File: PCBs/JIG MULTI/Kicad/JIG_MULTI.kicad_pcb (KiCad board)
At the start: 2 copper layers, 107.9 x 78.7 mm, 19 parts, among them U1 Vita_Connector, U2 12pad, U3 12pad

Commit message: fixed silkscreen typo
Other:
- board text added: "5V R1 = 1K R2 = 1K R3 = 1K R4 = 150 R5 = 2K R6 = 7.5K"
- board text removed: "5V R1 = 1K R2 = 1K R3 = 1K R4 = 150 R5 = 2K R5 = 7.5K"
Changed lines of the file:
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@@
   (gr_rect (start 31.75 30.48) (end 139.7 109.22)
     (stroke (width 0.1) (type default)) (fill none) (layer "Edge.Cuts"))
-  (gr_text "5V\nR1 = 1K\nR2 = 1K\nR3 = 1K\nR4 = 150\nR5 = 2K\nR5 = 7.5K" (at 134.62 55.88) (layer "B.SilkS")
+  (gr_text "5V\nR1 = 1K\nR2 = 1K\nR3 = 1K\nR4 = 150\nR5 = 2K\nR6 = 7.5K" (at 134.62 55.88) (layer "B.SilkS")
     (effects (font (size 2 2) (thickness 0.1)) (justify left bottom mirror))
   )
@@
     (effects (font (size 1 1) (thickness 0.2)) (justify left bottom))
   )
-  (gr_text "5V\nR1 = 1K\nR2 = 1K\nR3 = 1K\nR4 = 150\nR5 = 2K\nR5 = 7.5K" (at 121.92 106.68) (layer "F.SilkS")
+  (gr_text "5V\nR1 = 1K\nR2 = 1K\nR3 = 1K\nR4 = 150\nR5 = 2K\nR6 = 7.5K" (at 121.92 106.68) (layer "F.SilkS")
     (effects (font (size 2 2) (thickness 0.1)) (justify left bottom))
   )

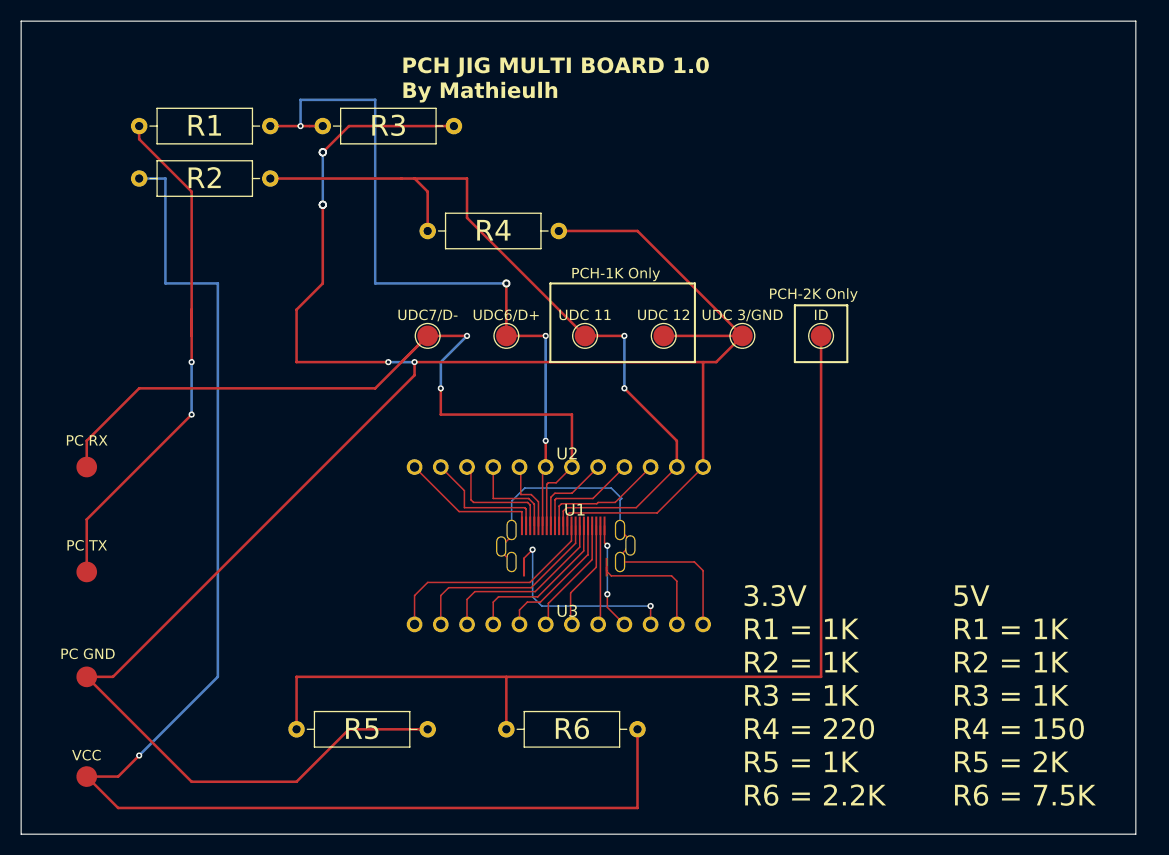
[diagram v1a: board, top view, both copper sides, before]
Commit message: smaller footprint
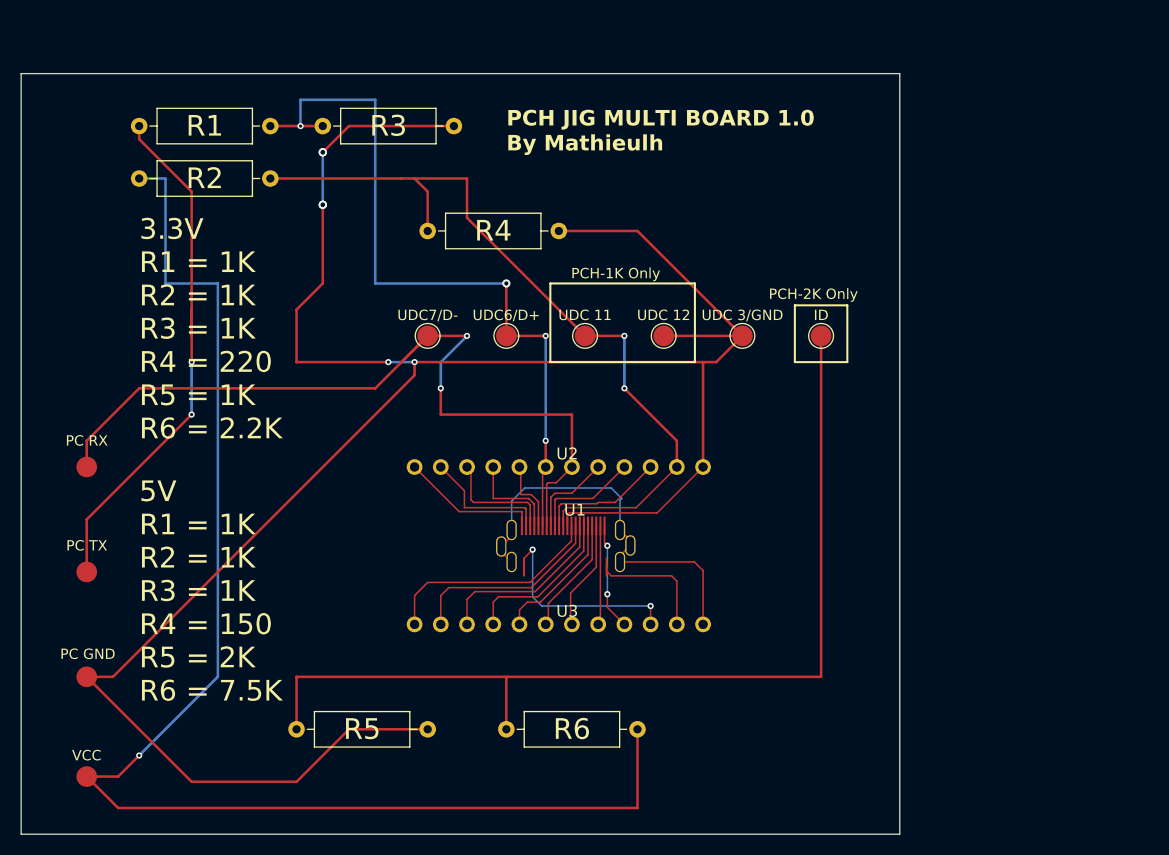
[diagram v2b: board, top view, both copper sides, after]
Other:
- board size 107.9 x 78.7 mm -> 85.1 x 73.7 mm
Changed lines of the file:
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@@
   (gr_rect (start 83 55.88) (end 97 63.5)
     (stroke (width 0.2) (type default)) (fill none) (layer "F.SilkS"))
-  (gr_rect (start 31.75 30.48) (end 139.7 109.22)
+  (gr_rect (start 31.75 35.56) (end 116.84 109.22)
     (stroke (width 0.1) (type default)) (fill none) (layer "Edge.Cuts"))
-  (gr_text "5V\nR1 = 1K\nR2 = 1K\nR3 = 1K\nR4 = 150\nR5 = 2K\nR6 = 7.5K" (at 134.62 55.88) (layer "B.SilkS")
+  (gr_text "5V\nR1 = 1K\nR2 = 1K\nR3 = 1K\nR4 = 150\nR5 = 2K\nR6 = 7.5K" (at 106.68 93.98) (layer "B.SilkS")
     (effects (font (size 2 2) (thickness 0.1)) (justify left bottom mirror))
   )
-  (gr_text "3.3V\nR1 = 1K\nR2 = 1K	\nR3 = 1K\nR4 = 220\nR5 = 1K\nR6 = 2.2K" (at 114.3 55.88) (layer "B.SilkS")
+  (gr_text "3.3V\nR1 = 1K\nR2 = 1K	\nR3 = 1K\nR4 = 220\nR5 = 1K\nR6 = 2.2K" (at 86.36 93.98) (layer "B.SilkS")
     (effects (font (size 2 2) (thickness 0.1)) (justify left bottom mirror))
   )
@@
     (effects (font (size 1 1) (thickness 0.2)) (justify left bottom))
   )
-  (gr_text "5V\nR1 = 1K\nR2 = 1K\nR3 = 1K\nR4 = 150\nR5 = 2K\nR6 = 7.5K" (at 121.92 106.68) (layer "F.SilkS")
+  (gr_text "5V\nR1 = 1K\nR2 = 1K\nR3 = 1K\nR4 = 150\nR5 = 2K\nR6 = 7.5K" (at 43.18 96.52) (layer "F.SilkS")
     (effects (font (size 2 2) (thickness 0.1)) (justify left bottom))
   )
@@
     (effects (font (size 1 1) (thickness 0.2)) (justify left bottom))
   )
-  (gr_text "3.3V\nR1 = 1K\nR2 = 1K	\nR3 = 1K\nR4 = 220\nR5 = 1K\nR6 = 2.2K" (at 101.6 106.68) (layer "F.SilkS")
+  (gr_text "3.3V\nR1 = 1K\nR2 = 1K	\nR3 = 1K\nR4 = 220\nR5 = 1K\nR6 = 2.2K" (at 43.18 71.12) (layer "F.SilkS")
     (effects (font (size 2 2) (thickness 0.1)) (justify left bottom))
   )
@@
     (effects (font (size 1 1) (thickness 0.15)))
   )
-  (gr_text "PCH JIG MULTI BOARD 1.0\nBy Mathieulh" (at 68.58 38.1) (layer "F.SilkS")
+  (gr_text "PCH JIG MULTI BOARD 1.0\nBy Mathieulh" (at 78.74 43.18) (layer "F.SilkS")
     (effects (font (size 1.5 1.5) (thickness 0.3) bold) (justify left bottom))
   )

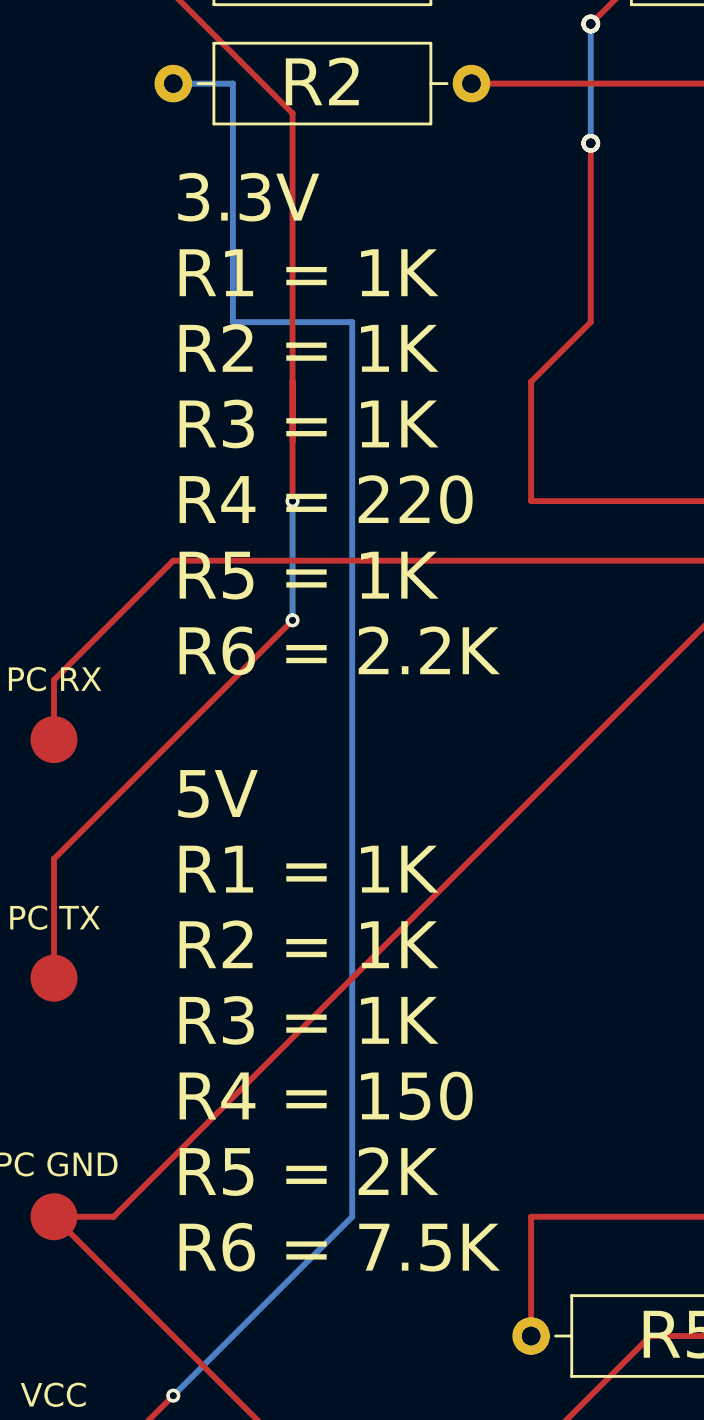
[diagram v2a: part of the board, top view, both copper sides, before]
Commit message: better silkscreen placement
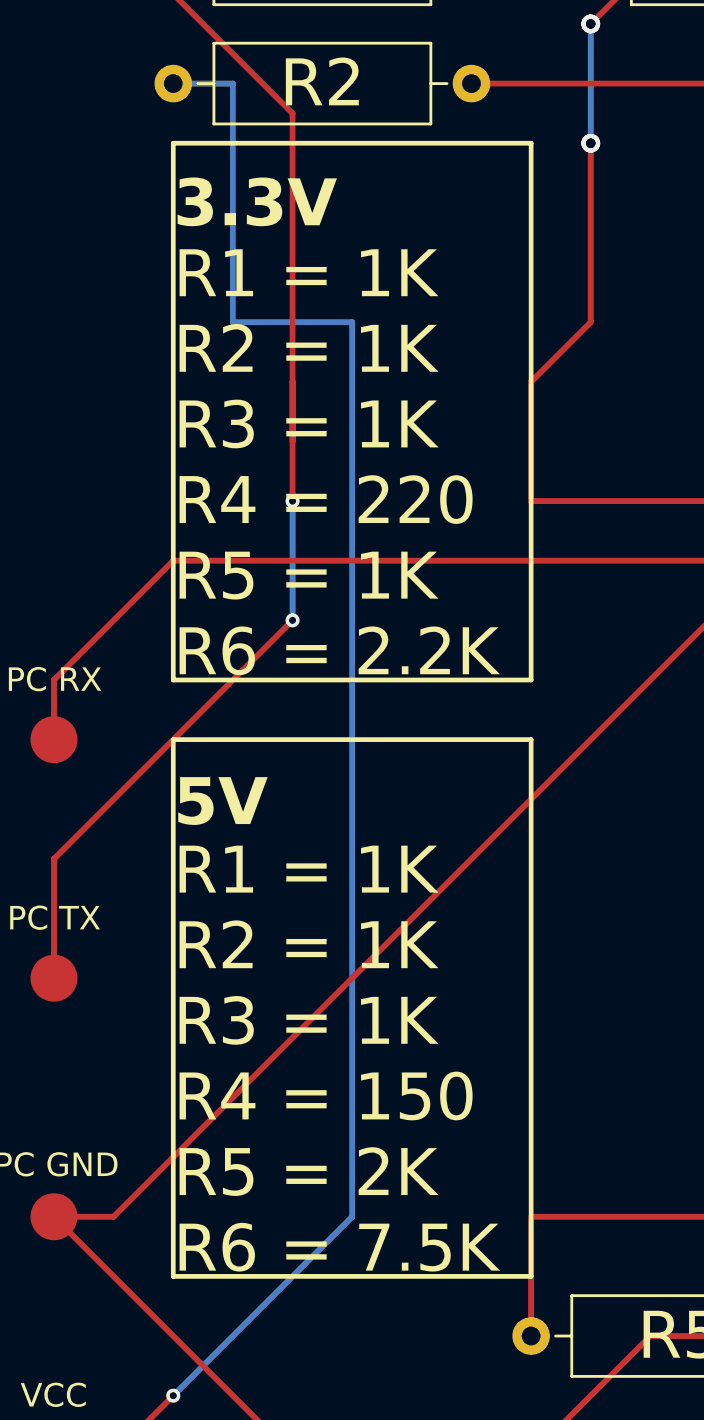
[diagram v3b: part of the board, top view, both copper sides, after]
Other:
- board text added: "3.3V"
- board text added: "5V"
- board text added: "R1 = 1K R2 = 1K R3 = 1K R4 = 150 R5 = 2K R6 = 7.5K"
- board text added: "R1 = 1K R2 = 1K R3 = 1K R4 = 220 R5 = 1K R6 = 2.2K"
- board text removed: "3.3V R1 = 1K R2 = 1K R3 = 1K R4 = 220 R5 = 1K R6 = 2.2K"
- board text removed: "5V R1 = 1K R2 = 1K R3 = 1K R4 = 150 R5 = 2K R6 = 7.5K"
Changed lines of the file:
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@@
   (gr_line (start 58.42 93.98) (end 58.42 99.06)
     (stroke (width 0.25) (type default)) (layer "F.Cu"))
+  (gr_rect (start 91.44 73.66) (end 106.68 96.52)
+    (stroke (width 0.2) (type default)) (fill none) (layer "B.SilkS"))
+  (gr_rect (start 91.44 48.26) (end 106.68 71.12)
+    (stroke (width 0.2) (type default)) (fill none) (layer "B.SilkS"))
   (gr_rect (start 106.68 58) (end 111.76 63.5)
+    (stroke (width 0.2) (type default)) (fill none) (layer "F.SilkS"))
+  (gr_rect (start 43.18 73.66) (end 58.42 96.52)
+    (stroke (width 0.2) (type default)) (fill none) (layer "F.SilkS"))
+  (gr_rect (start 43.18 48.26) (end 58.42 71.12)
     (stroke (width 0.2) (type default)) (fill none) (layer "F.SilkS"))
   (gr_rect (start 83 55.88) (end 97 63.5)
@@
   (gr_rect (start 31.75 35.56) (end 116.84 109.22)
     (stroke (width 0.1) (type default)) (fill none) (layer "Edge.Cuts"))
-  (gr_text "5V\nR1 = 1K\nR2 = 1K\nR3 = 1K\nR4 = 150\nR5 = 2K\nR6 = 7.5K" (at 106.68 93.98) (layer "B.SilkS")
+  (gr_text "5V" (at 106.68 77.5) (layer "B.SilkS")
+    (effects (font (size 2 2) (thickness 0.4) bold) (justify left bottom mirror))
+  )
+  (gr_text "R1 = 1K\nR2 = 1K\nR3 = 1K\nR4 = 150\nR5 = 2K\nR6 = 7.5K" (at 106.68 96.52) (layer "B.SilkS")
     (effects (font (size 2 2) (thickness 0.1)) (justify left bottom mirror))
   )
-  (gr_text "3.3V\nR1 = 1K\nR2 = 1K	\nR3 = 1K\nR4 = 220\nR5 = 1K\nR6 = 2.2K" (at 86.36 93.98) (layer "B.SilkS")
+  (gr_text "R1 = 1K\nR2 = 1K	\nR3 = 1K\nR4 = 220\nR5 = 1K\nR6 = 2.2K" (at 106.68 71.12) (layer "B.SilkS")
     (effects (font (size 2 2) (thickness 0.1)) (justify left bottom mirror))
+  )
+  (gr_text "3.3V" (at 106.68 52) (layer "B.SilkS")
+    (effects (font (size 2 2) (thickness 0.4) bold) (justify left bottom mirror))
   )
   (gr_text "PC GND" (at 38.202681 91.783349) (layer "F.SilkS")
@@
     (effects (font (size 1 1) (thickness 0.2)) (justify left bottom))
   )
-  (gr_text "5V\nR1 = 1K\nR2 = 1K\nR3 = 1K\nR4 = 150\nR5 = 2K\nR6 = 7.5K" (at 43.18 96.52) (layer "F.SilkS")
+  (gr_text "R1 = 1K\nR2 = 1K\nR3 = 1K\nR4 = 150\nR5 = 2K\nR6 = 7.5K" (at 43.18 96.52) (layer "F.SilkS")
     (effects (font (size 2 2) (thickness 0.1)) (justify left bottom))
   )
@@
     (effects (font (size 1 1) (thickness 0.2)) (justify left bottom))
   )
-  (gr_text "3.3V\nR1 = 1K\nR2 = 1K	\nR3 = 1K\nR4 = 220\nR5 = 1K\nR6 = 2.2K" (at 43.18 71.12) (layer "F.SilkS")
+  (gr_text "R1 = 1K\nR2 = 1K	\nR3 = 1K\nR4 = 220\nR5 = 1K\nR6 = 2.2K" (at 43.18 71.12) (layer "F.SilkS")
     (effects (font (size 2 2) (thickness 0.1)) (justify left bottom))
   )
   (gr_text "PC TX" (at 38.1 81.28) (layer "F.SilkS")
     (effects (font (size 1 1) (thickness 0.15)))
+  )
+  (gr_text "3.3V" (at 43.18 52) (layer "F.SilkS")
+    (effects (font (size 2 2) (thickness 0.4) bold) (justify left bottom))
   )
   (gr_text "VCC" (at 38.1 101.6) (layer "F.SilkS")
@@
     (effects (font (size 1.5 1.5) (thickness 0.3) bold) (justify left bottom))
   )
+  (gr_text "5V" (at 43.18 77.5) (layer "F.SilkS")
+    (effects (font (size 2 2) (thickness 0.4) bold) (justify left bottom))
+  )
   (segment (start 81.788 86.233) (end 77.978 86.233) (width 0.15) (layer "F.Cu") (net 0))
